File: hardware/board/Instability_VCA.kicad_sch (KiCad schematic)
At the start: 42 parts

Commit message: hardware: minor fixes and aesthetic updates
- Fix HP LEDs being backwards
- Switch power header, pot, and jack footprints to longpad variants
- Make the text size on the front side larger
- Add "red" and "blue" text next to respective LEDs on front side
- Adjusted zone thermal spoke for better connection to GND pads
- Squished the solder jumpers for instability type closer together
- Minor adjustments to traces to accommodate longpad footprints
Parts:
- J?: footprint winterbloom:AudioJack_WQP518MA_Compact_S -> winterbloom:AudioJack_WQP518MA_Compact_S_LongPads
- RV?: footprint winterbloom:Potentiometer_Alpha_R0904N -> winterbloom:Potentiometer_Alpha_R0904N_LongPads
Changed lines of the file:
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@@
       (effects (font (size 1.27 1.27)) (justify left))
     )
-    (property "Footprint" "winterbloom:Potentiometer_Alpha_R0904N" (at 64.77 138.43 0)
+    (property "Footprint" "winterbloom:Potentiometer_Alpha_R0904N_LongPads" (at 64.77 138.43 0)
       (effects (font (size 1.27 1.27)) hide)
     )
@@
       (effects (font (size 1.27 1.27)))
     )
-    (property "Footprint" "winterbloom:AudioJack_WQP518MA_Compact_S" (at 30.48 106.68 0)
-      (effects (font (size 1.27 1.27)) hide)
-    )
+    (property "Footprint" "winterbloom:AudioJack_WQP518MA_Compact_S_LongPads" (at 30.48 106.68 0)
+      (effects (font (size 1.27 1.27)) hide)
+    )

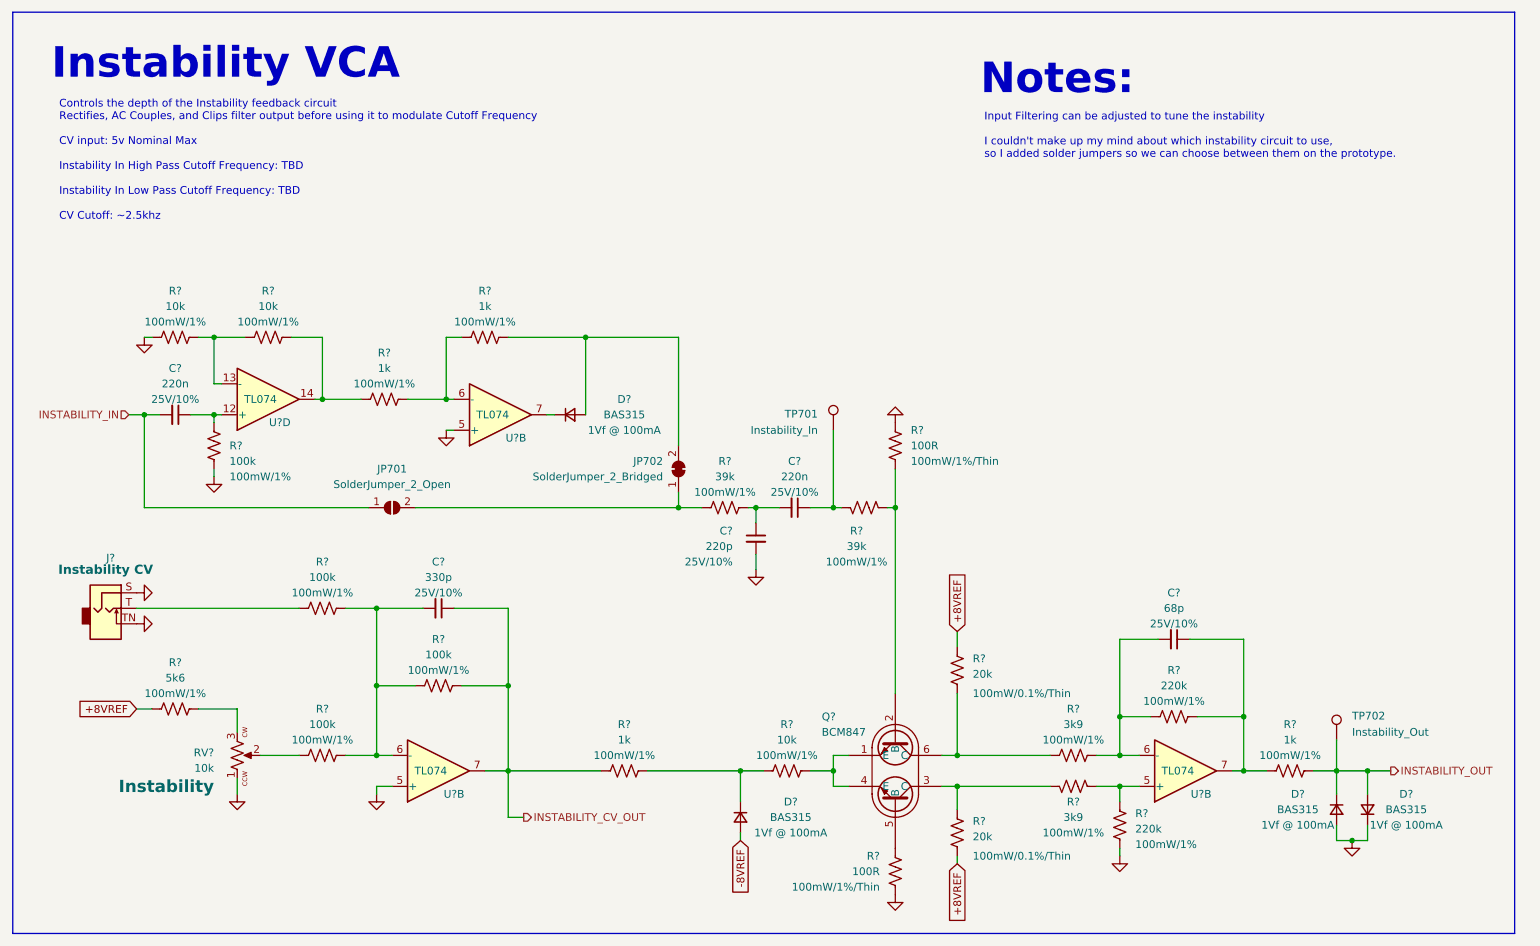
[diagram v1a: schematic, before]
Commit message: Updated Schematic
-Added R935, R936, and Q901 to make resonance self oscillation LED turn on sharply

-Moved D929, D930, and added R933, R934 to make FM1 LED more sensitive

-Changed FM1 Attenuverter and added R410 and R411 to make FM1 Knob have some curve/deadzone

-Changed Resonance VCA output and added R623 and R624 to make resonance VCA output higher voltage to avoid opamp offset being significant .

-Added testing documents
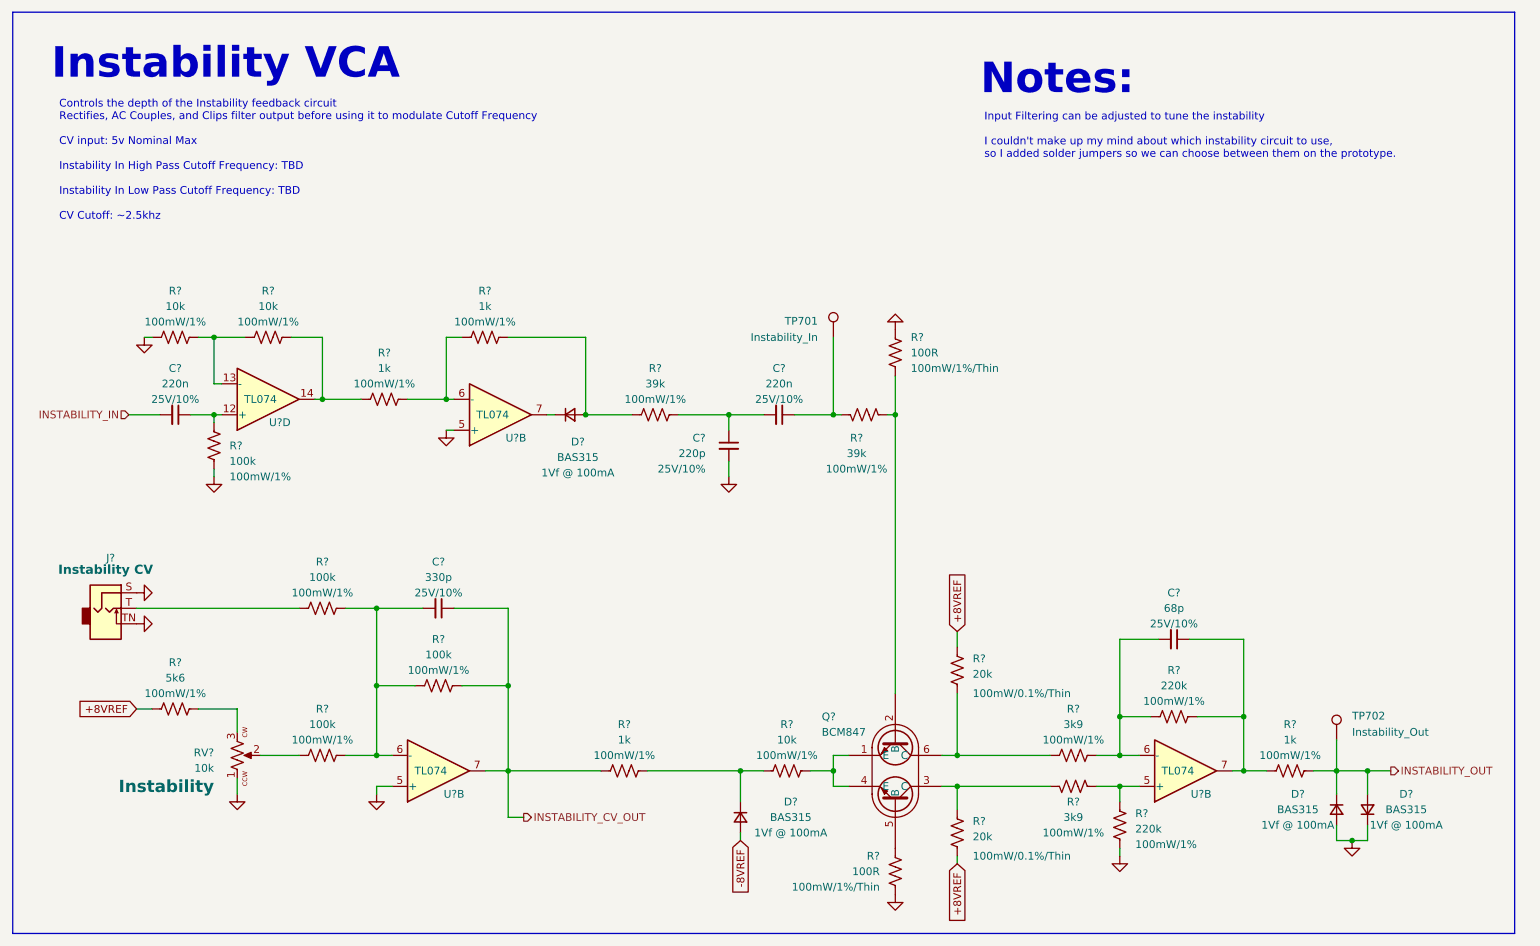
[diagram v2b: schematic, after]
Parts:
- removed JP701: SolderJumper_2_Open, Jumper:SolderJumper-2_P1.3mm_Open_RoundedPad1.0x1.5mm, symbol Jumper:SolderJumper_2_Open
- removed JP702: SolderJumper_2_Bridged, Jumper:SolderJumper-2_P1.3mm_Bridged_RoundedPad1.0x1.5mm, symbol Jumper:SolderJumper_2_Bridged
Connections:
- net at R?.2: now also D?.2 (A), R?.1
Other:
- moved on the sheet: C?, R?, TP701
